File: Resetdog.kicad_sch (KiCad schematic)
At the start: 18 parts, among them U14 MC14541BD, U15 MC74HC4538ADG, U20 74LVC1G17

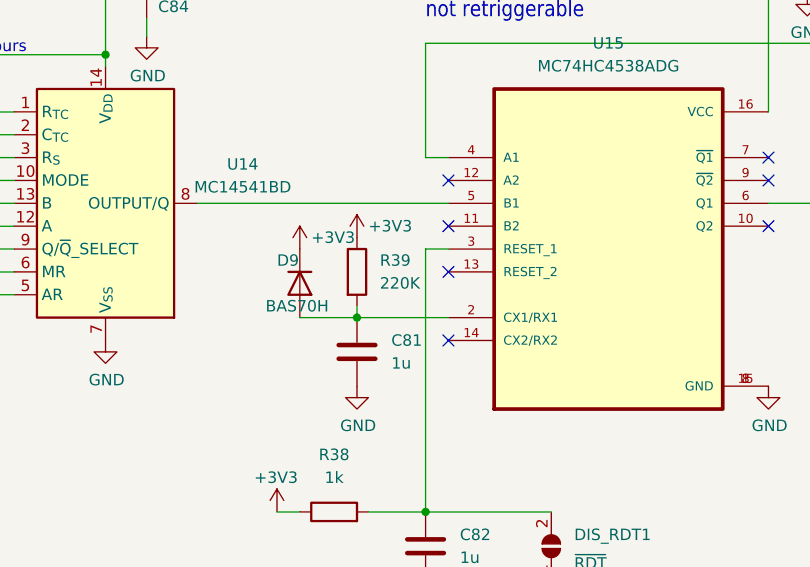
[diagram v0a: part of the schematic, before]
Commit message: Add latchup protection circuits
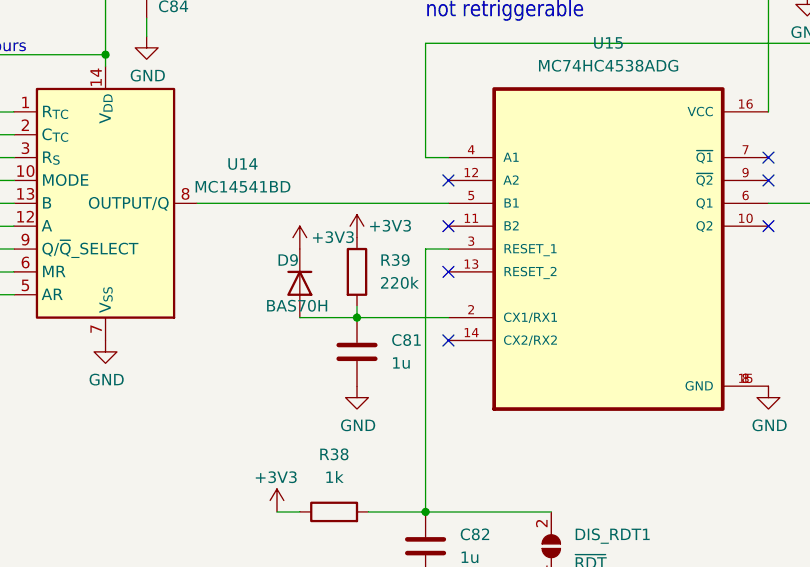
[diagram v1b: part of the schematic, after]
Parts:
- R39: value 220K -> 220k
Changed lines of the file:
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@@
       (effects (font (size 1.27 1.27)) (justify left))
     )
-    (property "Value" "220K" (id 1) (at 129.54 93.9799 0)
+    (property "Value" "220k" (id 1) (at 129.54 93.9799 0)
       (effects (font (size 1.27 1.27)) (justify left))
     )

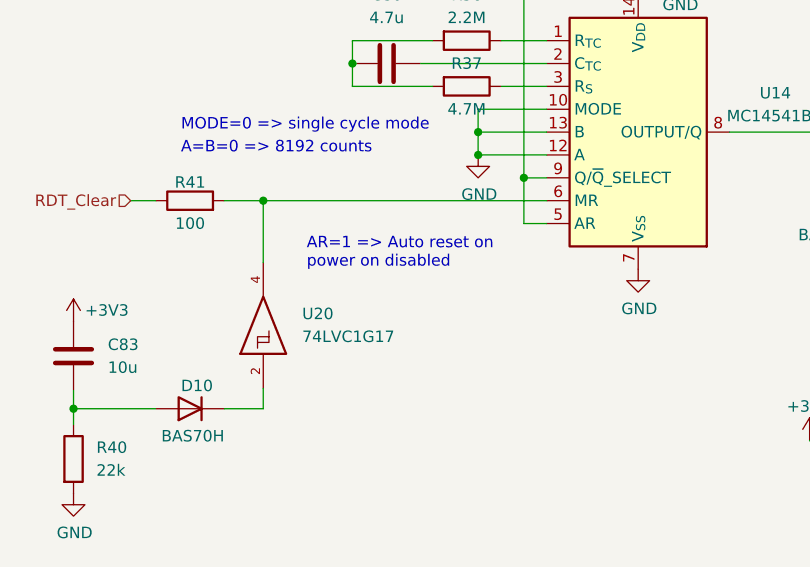
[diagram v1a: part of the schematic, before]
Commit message: Add for new lines to the UCI bus; plus minor fixes: introduce resistor in EDU_BOOT_Pin line, remove zener before DC-DC ~EN input
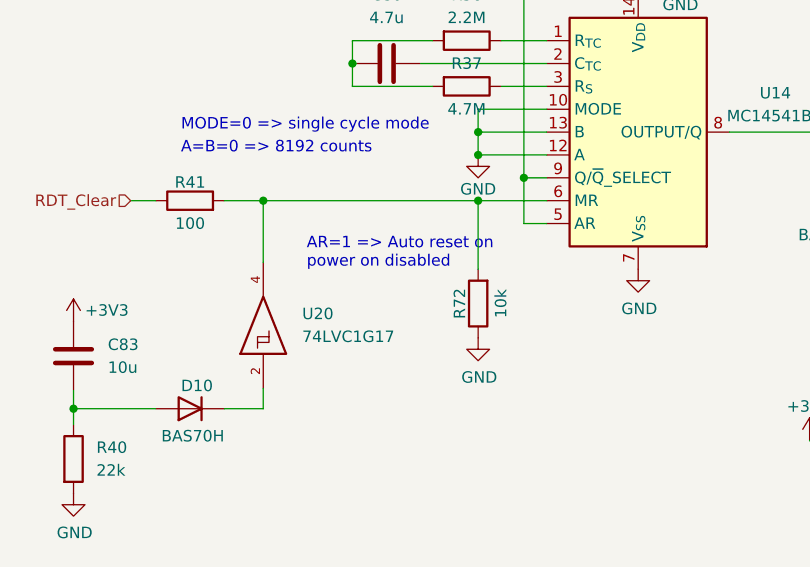
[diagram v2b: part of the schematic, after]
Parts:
- added R72: 10k, Resistor_SMD:R_0603_1608Metric, symbol Device:R
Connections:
- net GND: now also R72.1
- net at R41.2, U14.6 (MR), U20.4: now also R72.2
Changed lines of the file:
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@@
   (junction (at 86.36 90.17) (diameter 0) (color 0 0 0 0)
+  )
+  (junction (at 81.28 92.71) (diameter 0) (color 0 0 0 0)
   )
   (junction (at 127 97.79) (diameter 0) (color 0 0 0 0)
@@
     (stroke (width 0) (type default) (color 0 0 0 0))
   )
+  (wire (pts (xy 81.28 92.71) (xy 81.28 100.33))
+    (stroke (width 0) (type default) (color 0 0 0 0))
+  )
   (wire (pts (xy 180.34 85.09) (xy 180.34 67.31))
     (stroke (width 0) (type default) (color 0 0 0 0))
@@
     (stroke (width 0) (type default) (color 0 0 0 0))
   )
-  (wire (pts (xy 57.404 92.71) (xy 88.9 92.71))
+  (wire (pts (xy 57.404 92.71) (xy 81.28 92.71))
     (stroke (width 0) (type default) (color 0 0 0 0))
   )
@@
   )
   (wire (pts (xy 36.322 115.824) (xy 36.322 117.602))
+    (stroke (width 0) (type default) (color 0 0 0 0))
+  )
+  (wire (pts (xy 81.28 92.71) (xy 88.9 92.71))
     (stroke (width 0) (type default) (color 0 0 0 0))
   )
@@
     )
     (property "Datasheet" "~" (id 3) (at 103.632 60.706 0)
+      (effects (font (size 1.27 1.27)) hide)
+    )
+    (pin "1")
+    (pin "2")
+  )
+  (symbol (lib_id "Device:R") (at 81.28 104.14 180) (unit 1)
+    (in_bom yes) (on_board yes)
+    (property "Reference" "R72" (id 0) (at 79.248 104.14 90))
+    (property "Value" "10k" (id 1) (at 83.82 104.14 90))
+    (property "Footprint" "Resistor_SMD:R_0603_1608Metric" (id 2) (at 83.058 104.14 90)
+      (effects (font (size 1.27 1.27)) hide)
+    )
+    (property "Datasheet" "~" (id 3) (at 81.28 104.14 0)
       (effects (font (size 1.27 1.27)) hide)
     )
@@
     (pin "1")
   )
+  (symbol (lib_id "power:GND") (at 81.28 107.95 0) (unit 1)
+    (in_bom yes) (on_board yes)
+    (property "Reference" "#PWR0109" (id 0) (at 81.28 114.3 0)
+      (effects (font (size 1.27 1.27)) hide)
+    )
+    (property "Value" "GND" (id 1) (at 81.407 112.3442 0))
+    (property "Footprint" "" (id 2) (at 81.28 107.95 0)
+      (effects (font (size 1.27 1.27)) hide)
+    )
+    (property "Datasheet" "" (id 3) (at 81.28 107.95 0)
+      (effects (font (size 1.27 1.27)) hide)
+    )
+    (pin "1")
+  )
   (symbol (lib_id "power:GND") (at 134.62 127 0) (unit 1)
     (in_bom yes) (on_board yes)
@@
       (effects (font (size 1.27 1.27)) hide)
     )
-    (property "Value" "GND" (id 1) (at 81.407 92.0242 0))
+    (property "Value" "GND" (id 1) (at 81.28 91.44 0))
     (property "Footprint" "" (id 2) (at 81.28 87.63 0)
       (effects (font (size 1.27 1.27)) hide)

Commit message: Add manufacture number and JLCPCB part number to components
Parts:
- C80: JLCPCB Part # (none) -> C5969198; Manufacturer_Part_Number (none) -> CL10A475KP8NNWC
- C81, C82: JLCPCB Part # (none) -> C307479; Manufacturer_Part_Number (none) -> CL10B105KA8NFNC
- C83: Manufacturer_Part_Number (none) -> CL10A106KP8NQSC
- C84, C85: JLCPCB Part # (none) -> C1591; Manufacturer_Part_Number (none) -> CL10B104KB8NNNC
- D10, D9: JLCPCB Part # (none) -> C426766; Manufacturer_Part_Number (none) -> BAS70H,115
- R36: JLCPCB Part # (none) -> C2103911; Manufacturer_Part_Number (none) -> ESR03EZPF2204
- R37: JLCPCB Part # (none) -> C2103209; Manufacturer_Part_Number (none) -> ESR03EZPF4704
- R38: JLCPCB Part # (none) -> C4073186; Manufacturer_Part_Number (none) -> ERJ-H3EF1001V
- R39: JLCPCB Part # (none) -> C4285297; Manufacturer_Part_Number (none) -> ERJ-H3EF5102V
- R40: JLCPCB Part # (none) -> C4333453; Manufacturer_Part_Number (none) -> ERJ-H3GJ223V
- R41: JLCPCB Part # (none) -> C2074896; Manufacturer_Part_Number (none) -> CRS0603AFX-1000ELF
- R72: JLCPCB Part # (none) -> C4297913; Manufacturer_Part_Number (none) -> ERJ-H3EF1002V
- U14: JLCPCB Part # (none) -> C7292; Manufacturer_Part_Number (none) -> MC14541BDR2G
- U15: JLCPCB Part # (none) -> C7292; Manufacturer_Part_Number (none) -> MC74HC4538ADG
- U20: JLCPCB Part # (none) -> C3753751; Manufacturer_Part_Number (none) -> SN74LVC1G17DBVRE4
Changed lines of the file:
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@@
+      (effects (font (size 1.27 1.27)) hide)
+    )
+    (property "JLCPCB Part #" "C4285297" (id 4) (at 127 92.71 0)
+      (effects (font (size 1.27 1.27)) hide)
+    )
+    (property "Manufacturer_Part_Number" "ERJ-H3EF5102V" (id 5) (at 127 92.71 0)
       (effects (font (size 1.27 1.27)) hide)
     )
@@
     )
     (property "Datasheet" "~" (id 3) (at 103.632 60.706 0)
+      (effects (font (size 1.27 1.27)) hide)
+    )
+    (property "JLCPCB Part #" "C1591" (id 4) (at 103.632 60.706 0)
+      (effects (font (size 1.27 1.27)) hide)
+    )
+    (property "Manufacturer_Part_Number" "CL10B104KB8NNNC " (id 5) (at 103.632 60.706 0)
       (effects (font (size 1.27 1.27)) hide)
     )
@@
     )
     (property "Datasheet" "~" (id 3) (at 81.28 104.14 0)
+      (effects (font (size 1.27 1.27)) hide)
+    )
+    (property "JLCPCB Part #" "C4297913" (id 4) (at 81.28 104.14 0)
+      (effects (font (size 1.27 1.27)) hide)
+    )
+    (property "Manufacturer_Part_Number" "ERJ-H3EF1002V" (id 5) (at 81.28 104.14 0)
       (effects (font (size 1.27 1.27)) hide)
     )
@@
     )
     (property "Datasheet" "" (id 3) (at 154.94 90.17 0)
+      (effects (font (size 1.27 1.27)) hide)
+    )
+    (property "Manufacturer_Part_Number" "MC74HC4538ADG " (id 4) (at 154.94 90.17 0)
+      (effects (font (size 1.27 1.27)) hide)
+    )
+    (property "JLCPCB Part #" "C7292" (id 5) (at 154.94 90.17 0)
       (effects (font (size 1.27 1.27)) hide)
     )
@@
       (effects (font (size 1.27 1.27)) hide)
     )
+    (property "JLCPCB Part #" "C2074896" (id 4) (at 49.276 92.71 0)
+      (effects (font (size 1.27 1.27)) hide)
+    )
+    (property "Manufacturer_Part_Number" "CRS0603AFX-1000ELF" (id 5) (at 49.276 92.71 0)
+      (effects (font (size 1.27 1.27)) hide)
+    )
     (pin "1")
     (pin "2")
@@
     )
     (property "Datasheet" "~" (id 3) (at 134.62 123.19 0)
+      (effects (font (size 1.27 1.27)) hide)
+    )
+    (property "JLCPCB Part #" "C307479" (id 4) (at 134.62 123.19 0)
+      (effects (font (size 1.27 1.27)) hide)
+    )
+    (property "Manufacturer_Part_Number" "CL10B105KA8NFNC " (id 5) (at 134.62 123.19 0)
       (effects (font (size 1.27 1.27)) hide)
     )
@@
     )
     (property "Datasheet" "~" (id 3) (at 177.038 56.642 0)
+      (effects (font (size 1.27 1.27)) hide)
+    )
+    (property "JLCPCB Part #" "C1591" (id 4) (at 177.038 56.642 0)
+      (effects (font (size 1.27 1.27)) hide)
+    )
+    (property "Manufacturer_Part_Number" "CL10B104KB8NNNC " (id 5) (at 177.038 56.642 0)
       (effects (font (size 1.27 1.27)) hide)
     )
@@
       (effects (font (size 1.27 1.27)) hide)
     )
+    (property "JLCPCB Part #" "C2103209" (id 4) (at 80.01 80.01 0)
+      (effects (font (size 1.27 1.27)) hide)
+    )
+    (property "Manufacturer_Part_Number" "ESR03EZPF4704 " (id 5) (at 80.01 80.01 0)
+      (effects (font (size 1.27 1.27)) hide)
+    )
     (pin "1")
     (pin "2")
@@
       (effects (font (size 1.27 1.27)) hide)
     )
+    (property "JLCPCB Part #" "C4333453" (id 4) (at 36.322 121.412 0)
+      (effects (font (size 1.27 1.27)) hide)
+    )
+    (property "Manufacturer_Part_Number" "ERJ-H3GJ223V" (id 5) (at 36.322 121.412 0)
+      (effects (font (size 1.27 1.27)) hide)
+    )
     (pin "1")
     (pin "2")
@@
     )
     (property "Datasheet" "~" (id 3) (at 49.276 115.824 0)
+      (effects (font (size 1.27 1.27)) hide)
+    )
+    (property "Manufacturer_Part_Number" "BAS70H,115" (id 4) (at 49.276 115.824 0)
+      (effects (font (size 1.27 1.27)) hide)
+    )
+    (property "JLCPCB Part #" "C426766" (id 5) (at 49.276 115.824 0)
       (effects (font (size 1.27 1.27)) hide)
     )
@@
     )
     (property "Datasheet" "~" (id 3) (at 120.65 93.98 0)
+      (effects (font (size 1.27 1.27)) hide)
+    )
+    (property "Manufacturer_Part_Number" "BAS70H,115 " (id 4) (at 120.65 93.98 90)
+      (effects (font (size 1.27 1.27)) hide)
+    )
+    (property "JLCPCB Part #" "C426766" (id 5) (at 120.65 93.98 90)
       (effects (font (size 1.27 1.27)) hide)
     )
@@
     )
     (property "Datasheet" "https://www.onsemi.com/pdf/datasheet/mc14541b-d.pdf" (id 3) (at 99.06 85.09 0)
+      (effects (font (size 1.27 1.27)) hide)
+    )
+    (property "Manufacturer_Part_Number" "MC14541BDR2G " (id 4) (at 99.06 85.09 0)
+      (effects (font (size 1.27 1.27)) hide)
+    )
+    (property "JLCPCB Part #" "C7292" (id 5) (at 99.06 85.09 0)
       (effects (font (size 1.27 1.27)) hide)
     )
@@
       (effects (font (size 1.27 1.27)) hide)
     )
+    (property "Manufacturer_Part_Number" "SN74LVC1G17DBVRE4 " (id 4) (at 57.404 105.918 90)
+      (effects (font (size 1.27 1.27)) hide)
+    )
+    (property "JLCPCB Part #" "C3753751" (id 5) (at 57.404 105.918 90)
+      (effects (font (size 1.27 1.27)) hide)
+    )
     (pin "2")
     (pin "3")
@@
       (effects (font (size 1.27 1.27)) hide)
     )
+    (property "JLCPCB Part #" "C4073186" (id 4) (at 124.46 119.38 0)
+      (effects (font (size 1.27 1.27)) hide)
+    )
+    (property "Manufacturer_Part_Number" "ERJ-H3EF1001V " (id 5) (at 124.46 119.38 0)
+      (effects (font (size 1.27 1.27)) hide)
+    )
     (pin "1")
     (pin "2")
@@
     )
     (property "Datasheet" "~" (id 3) (at 36.322 109.982 0)
+      (effects (font (size 1.27 1.27)) hide)
+    )
+    (property "Manufacturer_Part_Number" "CL10A106KP8NQSC " (id 4) (at 36.322 109.982 0)
       (effects (font (size 1.27 1.27)) hide)
     )
@@
       (effects (font (size 1.27 1.27)) hide)
     )
+    (property "JLCPCB Part #" "C5969198" (id 4) (at 71.12 77.47 0)
+      (effects (font (size 1.27 1.27)) hide)
+    )
+    (property "Manufacturer_Part_Number" "CL10A475KP8NNWC " (id 5) (at 71.12 77.47 0)
+      (effects (font (size 1.27 1.27)) hide)
+    )
     (pin "1")
     (pin "2")
@@
     )
     (property "Datasheet" "~" (id 3) (at 127 101.6 0)
+      (effects (font (size 1.27 1.27)) hide)
+    )
+    (property "JLCPCB Part #" "C307479" (id 4) (at 127 101.6 0)
+      (effects (font (size 1.27 1.27)) hide)
+    )
+    (property "Manufacturer_Part_Number" "CL10B105KA8NFNC " (id 5) (at 127 101.6 0)
       (effects (font (size 1.27 1.27)) hide)
     )
@@
       (effects (font (size 1.27 1.27)) hide)
     )
+    (property "JLCPCB Part #" "C2103911" (id 4) (at 80.01 74.93 0)
+      (effects (font (size 1.27 1.27)) hide)
+    )
+    (property "Manufacturer_Part_Number" "ESR03EZPF2204 " (id 5) (at 80.01 74.93 0)
+      (effects (font (size 1.27 1.27)) hide)
+    )

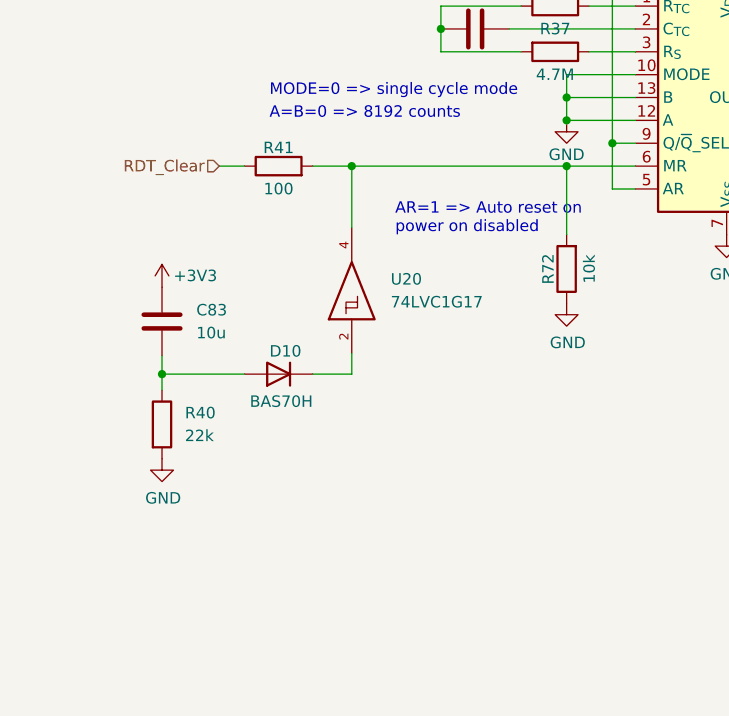
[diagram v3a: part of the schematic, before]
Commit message: Change symbol for U20 Schmitt trigger
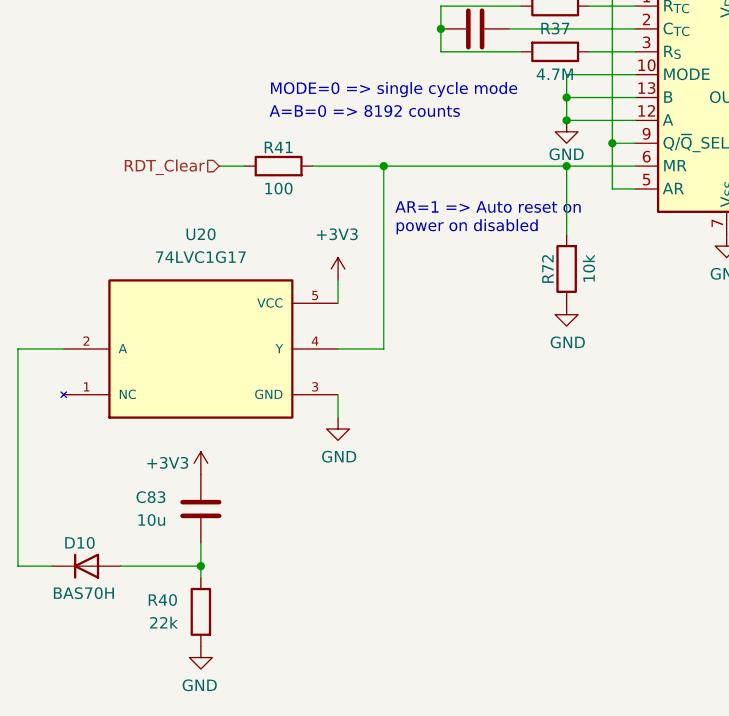
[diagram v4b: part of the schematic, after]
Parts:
- U20: symbol 74xGxx:74LVC1G17 -> STS1_COBC_V2-rescue:74LVC1G17GW_125; Availability (none) -> In Stock; Check_prices (none) -> https://www.snapeda.com/parts/74LVC1G17GW,125/Nexperia/view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; MF (none) -> Nexperia; MP (none) -> 74LVC1G17GW,125; Package (none) -> SOT-353 Nexperia USA; Price (none) -> None; Purchase-URL (none) -> https://www.snapeda.com/api/url_track_click_mouser/?unipart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; SnapEDA_Link (none) -> https://www.snapeda.com/parts/74LVC1G17GW,125/Nexperia/view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
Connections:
- net VCC is gone; now on net +3V3: U20.5 (VCC)
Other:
- moved on the sheet: C83, D10, R40

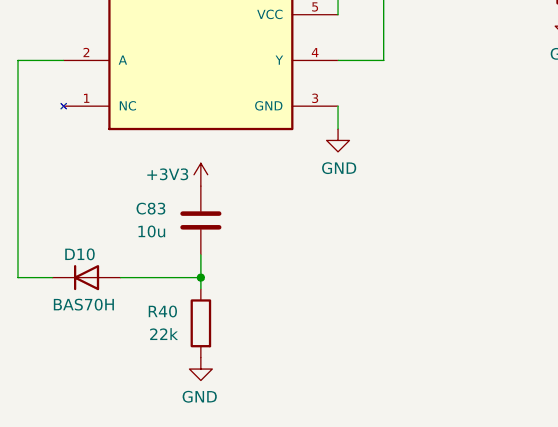
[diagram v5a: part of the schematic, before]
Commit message: Make a jump-start pulse for RTD shorter: R40 22 kOhm -> 10 kOhm, C83 10 uF -> 47 nF
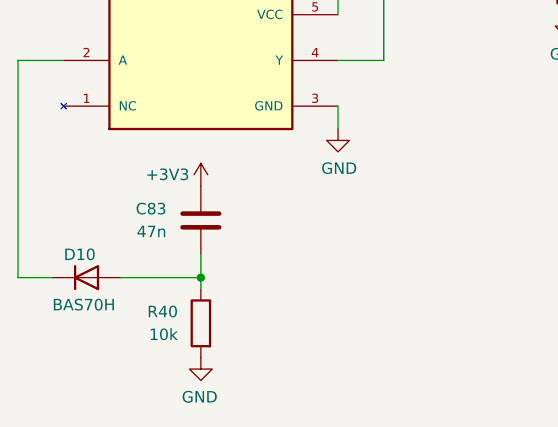
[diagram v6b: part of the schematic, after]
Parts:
- C83: value 10u -> 47n; Manufacturer_Part_Number CL10A106KP8NQSC -> CL10B473KB8VPJC
- R40: value 22k -> 10k; JLCPCB Part # C4333453 -> C4297913; Manufacturer_Part_Number ERJ-H3GJ223V -> ERJ-H3EF1002V
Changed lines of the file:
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@@
       (effects (font (size 1.27 1.27)) (justify left))
     )
-    (property "Value" "22k" (id 1) (at 38.1 143.5099 0)
+    (property "Value" "10k" (id 1) (at 38.1 143.5099 0)
       (effects (font (size 1.27 1.27)) (justify left))
     )
@@
       (effects (font (size 1.27 1.27)) hide)
     )
-    (property "JLCPCB Part #" "C4333453" (id 4) (at 40.64 142.24 0)
-      (effects (font (size 1.27 1.27)) hide)
-    )
-    (property "Manufacturer_Part_Number" "ERJ-H3GJ223V" (id 5) (at 40.64 142.24 0)
+    (property "JLCPCB Part #" "C4297913" (id 4) (at 40.64 142.24 0)
+      (effects (font (size 1.27 1.27)) hide)
+    )
+    (property "Manufacturer_Part_Number" "ERJ-H3EF1002V" (id 5) (at 40.64 142.24 0)
       (effects (font (size 1.27 1.27)) hide)
     )
@@
       (effects (font (size 1.27 1.27)) (justify left))
     )
-    (property "Value" "10u" (id 1) (at 36.83 132.0799 0)
+    (property "Value" "47n" (id 1) (at 36.83 132.0799 0)
       (effects (font (size 1.27 1.27)) (justify left))
     )
@@
       (effects (font (size 1.27 1.27)) hide)
     )
-    (property "Manufacturer_Part_Number" "CL10A106KP8NQSC " (id 4) (at 40.64 130.81 0)
-      (effects (font (size 1.27 1.27)) hide)
-    )
+    (property "Manufacturer_Part_Number" "CL10B473KB8VPJC " (id 4) (at 40.64 130.81 0)
+      (effects (font (size 1.27 1.27)) hide)
+    )
